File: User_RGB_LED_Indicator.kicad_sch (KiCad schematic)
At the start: 12 parts, among them IC901 SN74AHCT1G125DRLR, IC902 REG71050DRVT

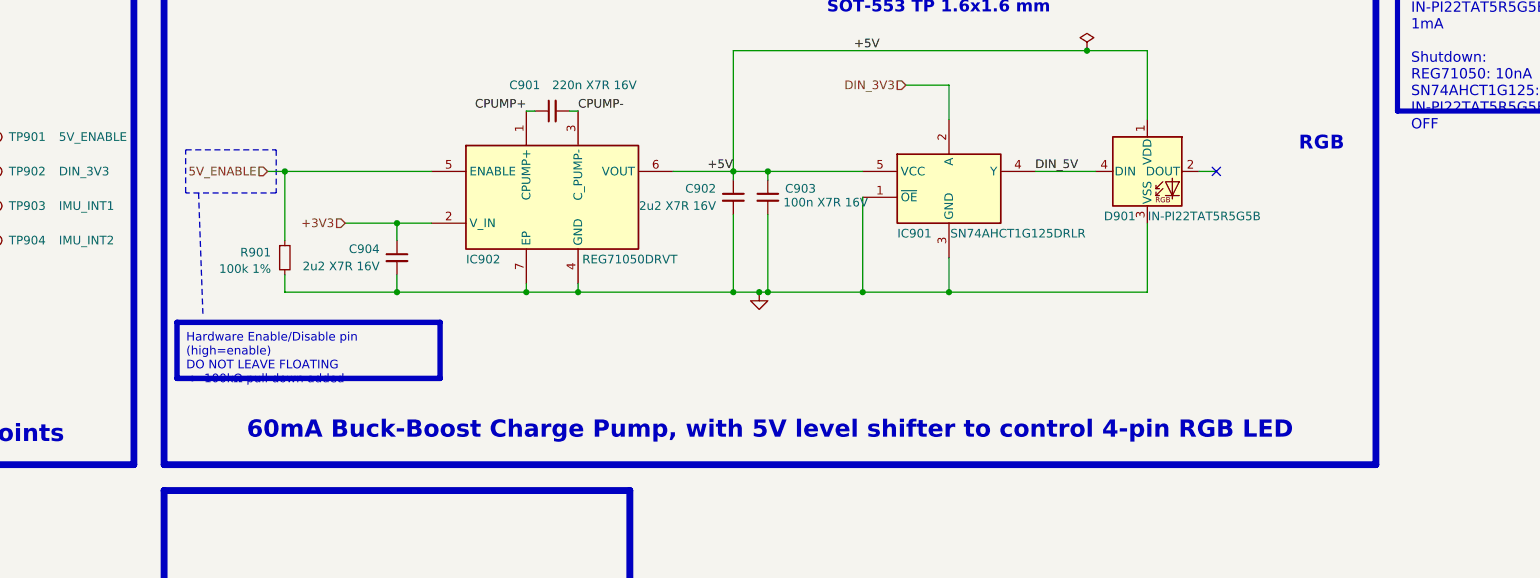
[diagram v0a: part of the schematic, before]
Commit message: Added PCB frame for assembly, almost finished auto-review, only MCU and motors left
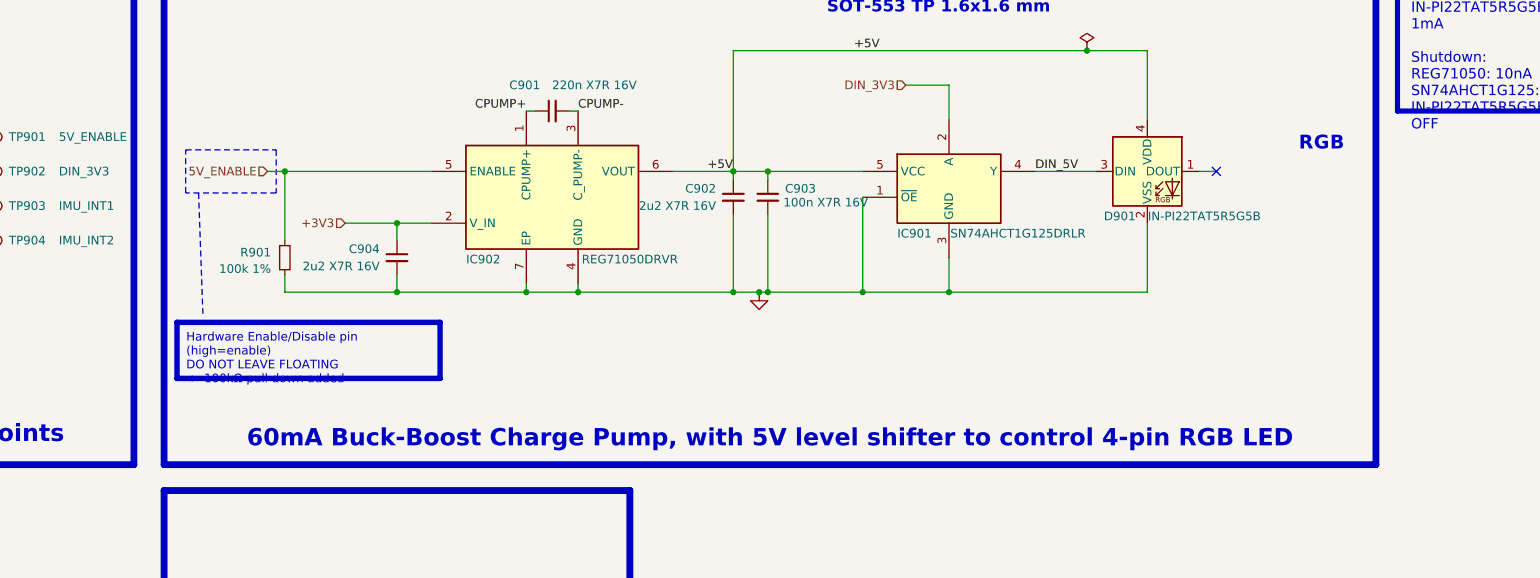
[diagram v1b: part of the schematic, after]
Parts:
- D901: symbol LED:WS2812B -> 0_Plume:IN-PI22TAT5R5G5B
- IC902: value REG71050DRVT -> REG71050DRVR
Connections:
- net +5V: now also D901.4 (VDD); no longer D901.1 (VDD)
- net DIN_5V: now also D901.3 (DIN); no longer D901.4 (DIN)
- net GND: now also D901.2 (VSS); no longer D901.3 (VSS)

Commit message: Final version, cleaned and ordered as is
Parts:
- C901: Manufacturer Murata Electronics -> TDK; Manufacturer Part Number GCM155R71C224KE02D -> CGA3E2X7R1C224K080AA; Supplier Part Number 81-GCM155R71C224KE2D -> 810-CGA3E2X7R1C224K
